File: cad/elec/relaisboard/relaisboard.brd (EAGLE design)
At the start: 34 x 23 mm, 28 parts, among them IC1 REG1117, T1 MMUN2233

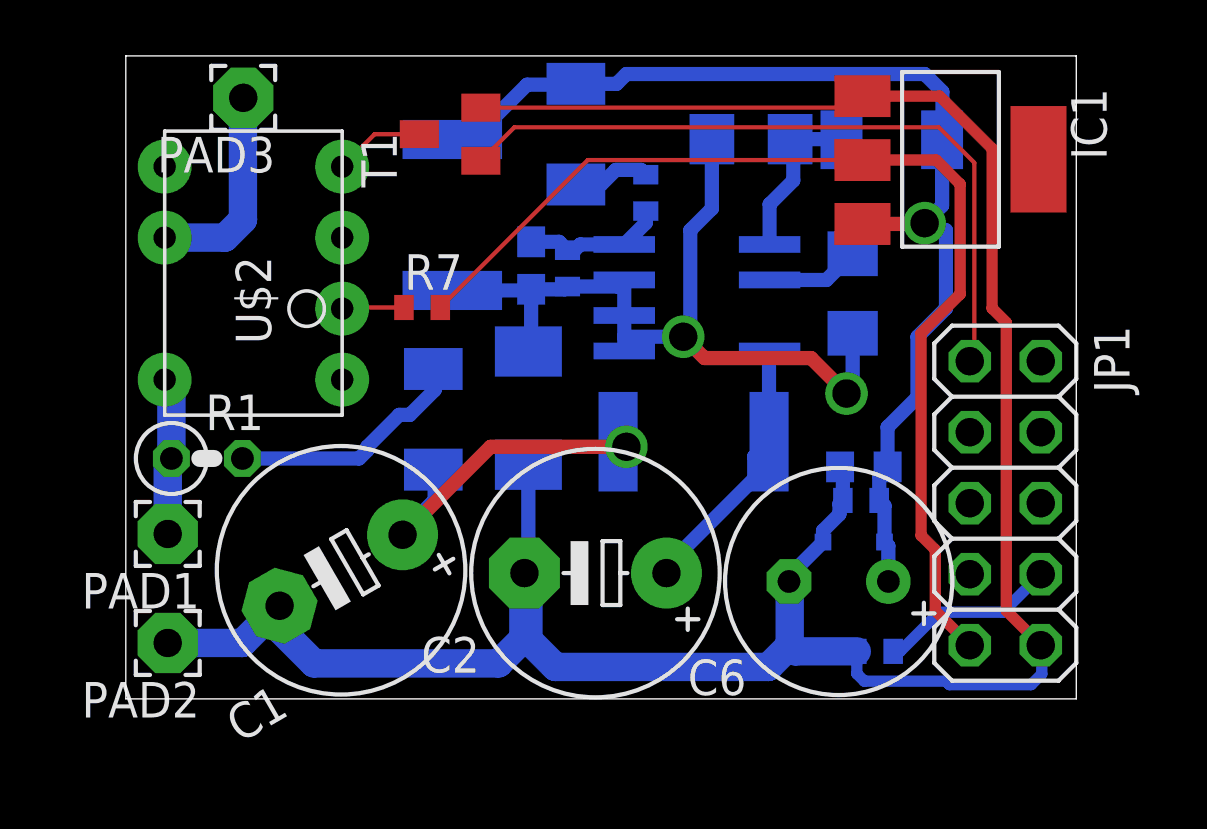
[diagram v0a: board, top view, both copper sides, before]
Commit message: changed track to be further away from cap
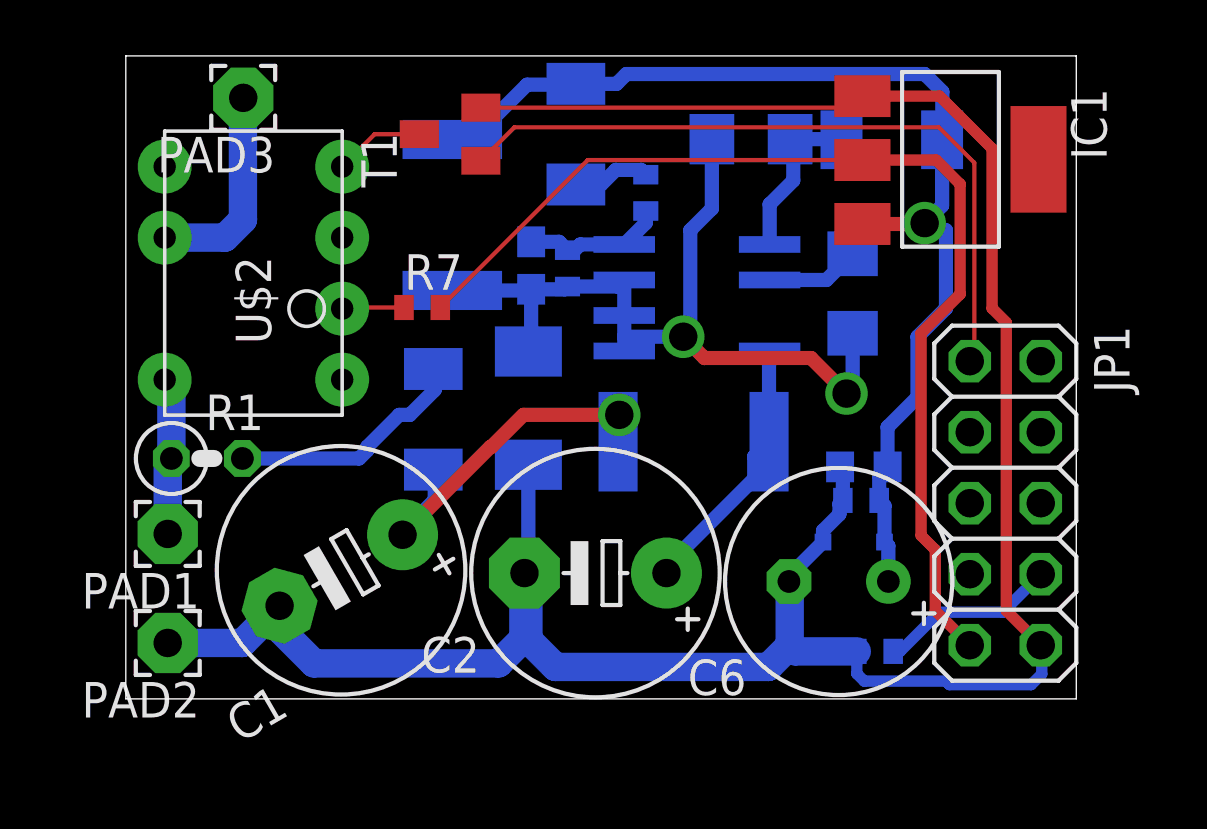
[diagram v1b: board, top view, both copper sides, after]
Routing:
- net N$2: track 12.5 -> 13.4 mm
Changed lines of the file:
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@@
 <setting verticaltext="up"/>
 </settings>
-<grid distance="5" unitdist="mil" unit="mil" style="lines" multiple="1" display="yes" altdistance="0.1" altunitdist="mm" altunit="mm"/>
+<grid distance="0.127" unitdist="mm" unit="mm" style="lines" multiple="1" display="yes" altdistance="0.1" altunitdist="mm" altunit="mm"/>
 <layers>
 <layer number="1" name="Top" color="4" fill="1" visible="yes" active="yes"/>
@@
 <wire x1="11.049" y1="8.151" x2="11" y2="8.2" width="0.508" layer="16"/>
 <wire x1="17.61" y1="9.2" x2="17.724" y2="9.2" width="0.508" layer="16"/>
-<wire x1="17.724" y1="9.2" x2="17.907" y2="9.017" width="0.508" layer="16"/>
-<via x="17.907" y="9.017" extent="1-16" drill="1.016"/>
-<wire x1="17.907" y1="9.017" x2="13.046703125" y2="9.017" width="0.508" layer="1"/>
+<wire x1="17.724" y1="9.2" x2="17.653" y2="10.16" width="0.508" layer="16"/>
+<via x="17.653" y="10.16" extent="1-16" drill="1.016"/>
 <wire x1="13.046703125" y1="9.017" x2="9.899703125" y2="5.87" width="0.508" layer="1"/>
+<wire x1="13.046703125" y1="9.017" x2="13.081" y2="9.017" width="0.508" layer="1"/>
+<wire x1="13.081" y1="9.017" x2="14.224" y2="10.16" width="0.508" layer="1"/>
+<wire x1="14.224" y1="10.16" x2="17.653" y2="10.16" width="0.508" layer="1"/>
 </signal>
 <signal name="N$3">
